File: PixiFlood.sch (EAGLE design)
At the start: 61 parts, among them IC1 L78LXXCU/BU, IC2 74LVC1G125DBV, IC3 LM1117-SOT223, IC4 WS2811SOP8, IC5 TC7W04FP-0.65, U1 PT4115B89E, U2 PT4115B89E, U3 PT4115B89E, X1 22-23-2041

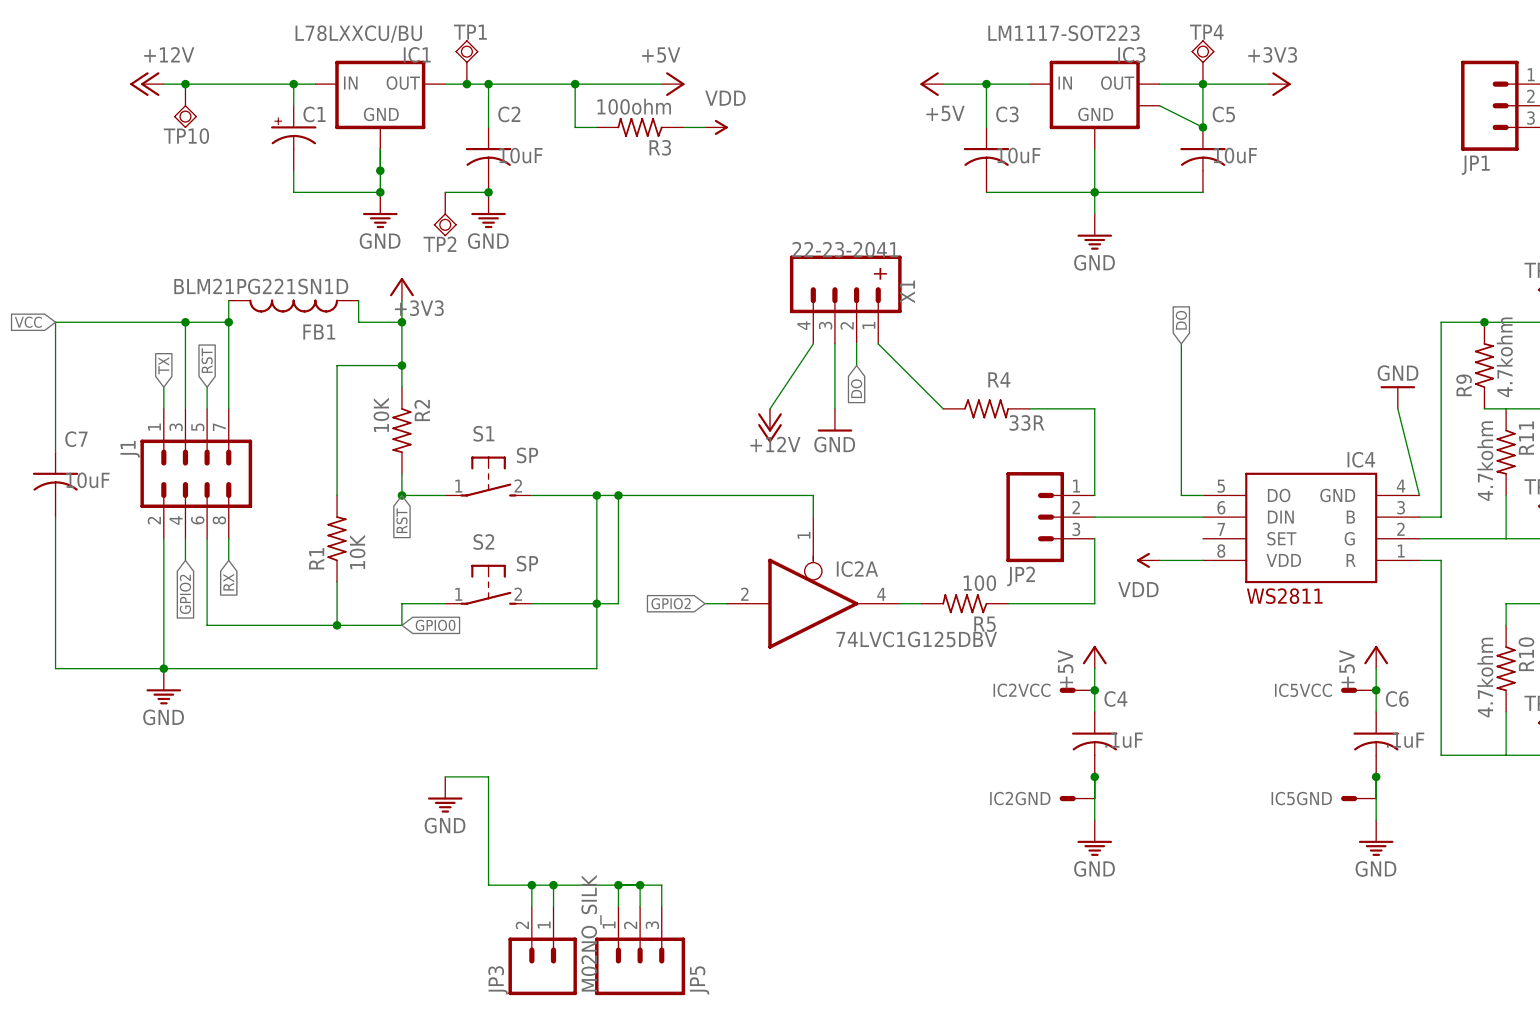
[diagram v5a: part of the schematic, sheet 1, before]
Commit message: Reworked layout
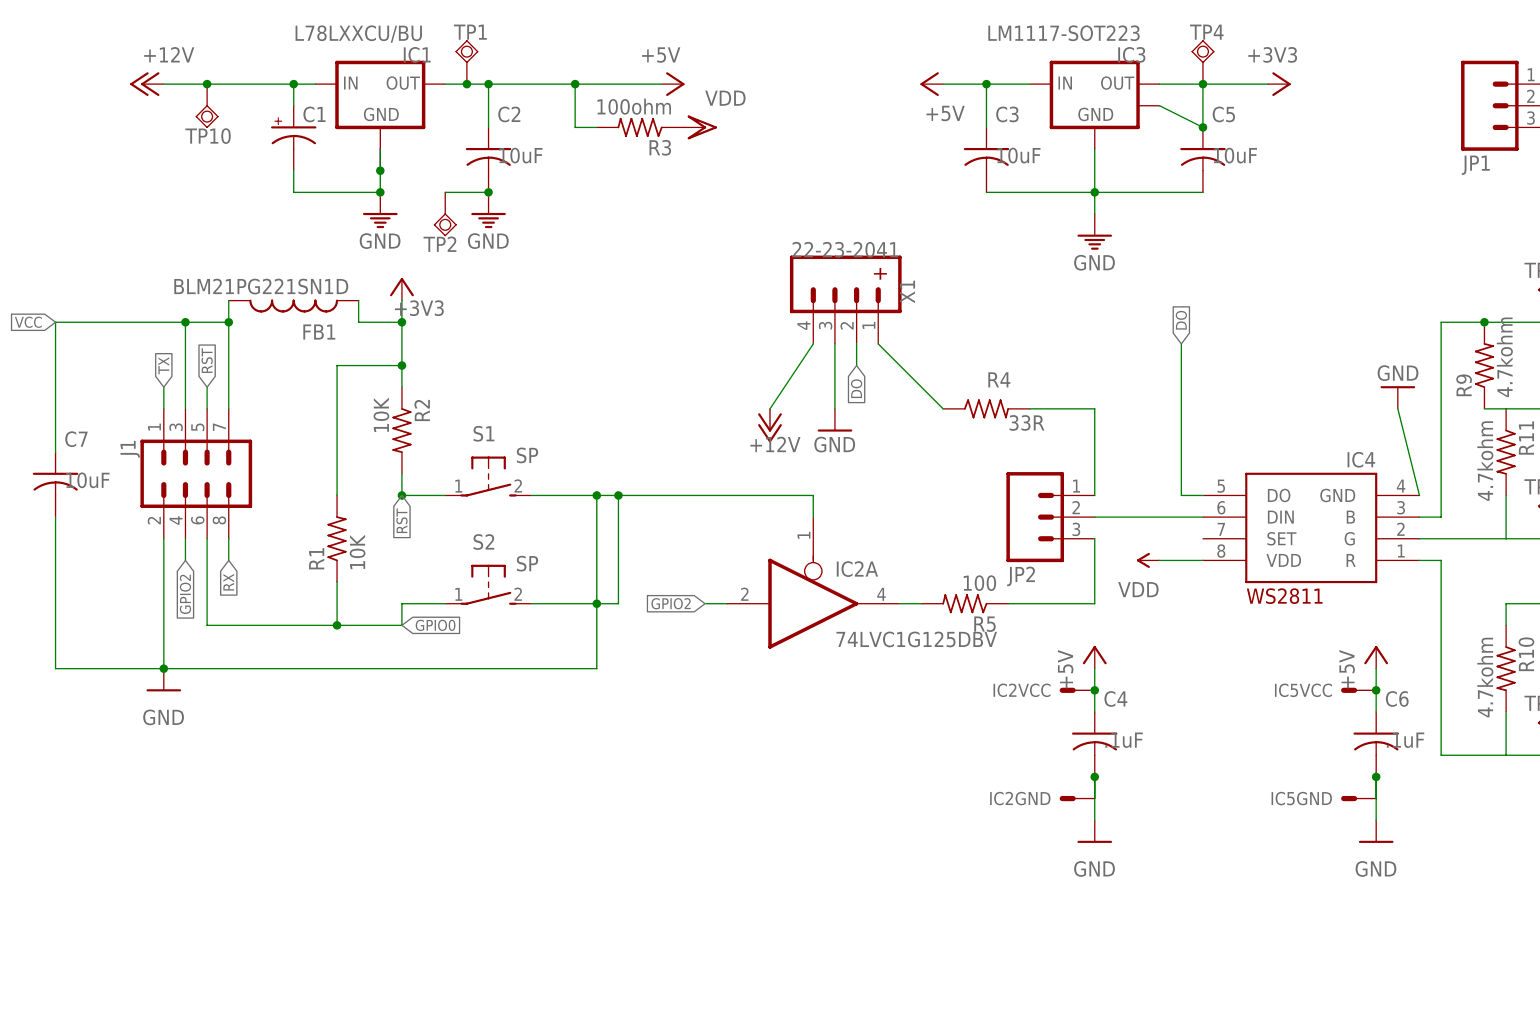
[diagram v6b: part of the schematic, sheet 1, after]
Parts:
- removed JP3: M02NO_SILK, connectors:M02NO_SILK
- removed JP5: (no value), connectors:M03LOCK_NO_SILK
- R3: device rcl:R-US_M0805 -> rcl:R-US_R0805
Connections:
- net GND: no longer JP3.1, JP3.2, JP5.1, JP5.2, JP5.3
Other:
- moved on the sheet: TP10
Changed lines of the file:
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@@
 <part name="P+1" library="supply1" library_urn="urn:adsk.eagle:library:371" deviceset="+12V" device=""/>
 <part name="P+2" library="supply1" library_urn="urn:adsk.eagle:library:371" deviceset="+5V" device=""/>
-<part name="R3" library="rcl" deviceset="R-US_" device="M0805" value="100ohm"/>
+<part name="R3" library="rcl" library_urn="urn:adsk.eagle:library:334" deviceset="R-US_" device="R0805" package3d_urn="urn:adsk.eagle:package:23553/2" value="100ohm"/>
 <part name="IC4" library="drivers" deviceset="WS2811" device="SOP8"/>
 <part name="R4" library="rcl" deviceset="R-US_" device="M1206" value="33R"/>
@@
 <part name="TP9" library="testpad" library_urn="urn:adsk.eagle:library:385" deviceset="TPSQ" device="PAD1-13" package3d_urn="urn:adsk.eagle:package:27946/1" value="TPSQPAD1-13"/>
 <part name="X1" library="connectors" deviceset="22-23-2041" device=""/>
-<part name="SUPPLY1" library="SparkFun-Aesthetics" deviceset="VDD" device=""/>
+<part name="SUPPLY1" library="supply1" library_urn="urn:adsk.eagle:library:371" deviceset="VDD" device=""/>
 <part name="SUPPLY2" library="SparkFun-Aesthetics" deviceset="VDD" device=""/>
 <part name="J1" library="connectors" deviceset="M04X2A" device=""/>
@@
 <part name="R2" library="resistors" deviceset="R-US_" device="R0805" value="10K"/>
 <part name="R5" library="resistors" deviceset="R-US_" device="R0805" value="100"/>
-<part name="GND1" library="supply" deviceset="GND" device=""/>
+<part name="GND1" library="supply1" library_urn="urn:adsk.eagle:library:371" deviceset="GND" device=""/>
 <part name="IC2" library="logic" deviceset="74*1G125" device="DBV" technology="LVC"/>
 <part name="P+5" library="supply1" library_urn="urn:adsk.eagle:library:371" deviceset="+5V" device=""/>
-<part name="GND6" library="supply" deviceset="GND" device=""/>
+<part name="GND6" library="supply1" library_urn="urn:adsk.eagle:library:371" deviceset="GND" device=""/>
 <part name="GND5" library="supply" deviceset="GND" device=""/>
 <part name="GND3" library="supply" deviceset="GND" device=""/>
-<part name="GND10" library="supply" deviceset="GND" device=""/>
-<part name="GND11" library="supply" deviceset="GND" device=""/>
-<part name="GND12" library="supply" deviceset="GND" device=""/>
+<part name="GND10" library="supply1" library_urn="urn:adsk.eagle:library:371" deviceset="GND" device=""/>
+<part name="GND11" library="supply1" library_urn="urn:adsk.eagle:library:371" deviceset="GND" device=""/>
+<part name="GND12" library="supply1" library_urn="urn:adsk.eagle:library:371" deviceset="GND" device=""/>
 <part name="JP2" library="connectors" deviceset="M03" device="LOCK"/>
 <part name="IC1" library="regulators" deviceset="L78LXXCU/BU" device=""/>
@@
 <part name="TP10" library="testpad" library_urn="urn:adsk.eagle:library:385" deviceset="TPSQ" device="PAD1-13" package3d_urn="urn:adsk.eagle:package:27946/1" value="TPSQPAD1-13"/>
 <part name="FB1" library="ELL-i-Passives" deviceset="FB" device="-0805-A" value="BLM21PG221SN1D"/>
-<part name="+3V33" library="supply" deviceset="+3V3" device=""/>
-<part name="+3V32" library="supply" deviceset="+3V3" device=""/>
+<part name="+3V33" library="supply1" library_urn="urn:adsk.eagle:library:371" deviceset="+3V3" device=""/>
+<part name="+3V32" library="supply1" library_urn="urn:adsk.eagle:library:371" deviceset="+3V3" device=""/>
 <part name="GND2" library="supply" deviceset="GND" device=""/>
 <part name="IC3" library="regulators" deviceset="LM1117" device="-SOT223"/>
@@
 <part name="P+6" library="supply1" library_urn="urn:adsk.eagle:library:371" deviceset="+5V" device=""/>
 <part name="C6" library="rcl" library_urn="urn:adsk.eagle:library:334" deviceset="C-US" device="C0805" package3d_urn="urn:adsk.eagle:package:23617/2" value=".1uF"/>
-<part name="GND7" library="supply" deviceset="GND" device=""/>
+<part name="GND7" library="supply1" library_urn="urn:adsk.eagle:library:371" deviceset="GND" device=""/>
 <part name="R9" library="rcl" deviceset="R-US_" device="M0805" value="4.7kohm"/>
 <part name="R10" library="rcl" deviceset="R-US_" device="M0805" value="4.7kohm"/>
@@
 <part name="TP15" library="testpad" library_urn="urn:adsk.eagle:library:385" deviceset="TPSQ" device="PAD1-13" package3d_urn="urn:adsk.eagle:package:27946/1" value="TPSQPAD1-13"/>
 <part name="TP16" library="testpad" library_urn="urn:adsk.eagle:library:385" deviceset="TPSQ" device="PAD1-13" package3d_urn="urn:adsk.eagle:package:27946/1" value="TPSQPAD1-13"/>
-<part name="GND9" library="supply" deviceset="GND" device=""/>
-<part name="JP3" library="connectors" deviceset="M02" device="NO_SILK"/>
-<part name="JP5" library="connectors" deviceset="M03" device="LOCK_NO_SILK"/>
 <part name="C1" library="rcl" library_urn="urn:adsk.eagle:library:334" deviceset="CPOL-US" device="UD-6,3X5,8" package3d_urn="urn:adsk.eagle:package:23471/1"/>
 </parts>
@@
 <attribute name="NAME" x="116.078" y="73.66" size="1.778" layer="95" rot="MR270"/>
 </instance>
-<instance part="SUPPLY1" gate="VDD" x="91.44" y="91.44" smashed="yes" rot="R270">
+<instance part="SUPPLY1" gate="G$1" x="91.44" y="91.44" smashed="yes" rot="R270">
 <attribute name="VALUE" x="91.44" y="93.98" size="1.778" layer="96"/>
 </instance>
@@
 <attribute name="TP_SIGNAL_NAME" x="147.32" y="100.33" size="1.778" layer="97" rot="R180"/>
 </instance>
-<instance part="TP10" gate="G$1" x="30.48" y="93.98" smashed="yes">
-<attribute name="NAME" x="27.94" y="89.535" size="1.778" layer="95"/>
-<attribute name="TP_SIGNAL_NAME" x="33.02" y="92.71" size="1.778" layer="97"/>
+<instance part="TP10" gate="G$1" x="33.02" y="93.98" smashed="yes">
+<attribute name="NAME" x="30.48" y="89.535" size="1.778" layer="95"/>
+<attribute name="TP_SIGNAL_NAME" x="35.56" y="92.71" size="1.778" layer="97"/>
 </instance>
 <instance part="FB1" gate="G$1" x="43.18" y="71.12" smashed="yes" rot="R180">
@@
 <attribute name="NAME" x="193.04" y="24.765" size="1.778" layer="95" rot="R180"/>
 <attribute name="TP_SIGNAL_NAME" x="187.96" y="21.59" size="1.778" layer="97" rot="R180"/>
-</instance>
-<instance part="GND9" gate="1" x="60.96" y="12.7" smashed="yes">
-<attribute name="VALUE" x="58.42" y="8.636" size="1.778" layer="96"/>
-</instance>
-<instance part="JP3" gate="G$1" x="73.66" y="-7.62" smashed="yes" rot="R90">
-<attribute name="VALUE" x="78.74" y="-10.16" size="1.778" layer="96" rot="R90"/>
-<attribute name="NAME" x="67.818" y="-10.16" size="1.778" layer="95" rot="R90"/>
-</instance>
-<instance part="JP5" gate="G$1" x="83.82" y="-7.62" smashed="yes" rot="MR90">
-<attribute name="VALUE" x="76.2" y="-10.16" size="1.778" layer="96" rot="MR90"/>
-<attribute name="NAME" x="89.662" y="-10.16" size="1.778" layer="95" rot="MR90"/>
 </instance>
 <instance part="C1" gate="G$1" x="43.18" y="91.44" smashed="yes">
@@
 <wire x1="170.18" y1="15.24" x2="170.18" y2="12.7" width="0.1524" layer="91"/>
 </segment>
-<segment>
-<pinref part="GND9" gate="1" pin="GND"/>
-<wire x1="60.96" y1="15.24" x2="66.04" y2="15.24" width="0.2032" layer="91"/>
-<wire x1="66.04" y1="15.24" x2="66.04" y2="2.54" width="0.2032" layer="91"/>
-<pinref part="JP3" gate="G$1" pin="2"/>
-<wire x1="66.04" y1="2.54" x2="71.12" y2="2.54" width="0.2032" layer="91"/>
-<wire x1="71.12" y1="0" x2="71.12" y2="2.54" width="0.2032" layer="91"/>
-<pinref part="JP3" gate="G$1" pin="1"/>
-<wire x1="71.12" y1="2.54" x2="73.66" y2="2.54" width="0.2032" layer="91"/>
-<wire x1="73.66" y1="2.54" x2="73.66" y2="0" width="0.2032" layer="91"/>
-<junction x="71.12" y="2.54"/>
-<junction x="73.66" y="2.54"/>
-<pinref part="JP5" gate="G$1" pin="3"/>
-<wire x1="73.66" y1="2.54" x2="83.82" y2="2.54" width="0.2032" layer="91"/>
-<wire x1="81.28" y1="2.54" x2="83.82" y2="2.54" width="0.2032" layer="91"/>
-<wire x1="83.82" y1="2.54" x2="86.36" y2="2.54" width="0.2032" layer="91"/>
-<wire x1="86.36" y1="2.54" x2="86.36" y2="0" width="0.2032" layer="91"/>
-<pinref part="JP5" gate="G$1" pin="2"/>
-<wire x1="83.82" y1="0" x2="83.82" y2="2.54" width="0.2032" layer="91"/>
-<pinref part="JP5" gate="G$1" pin="1"/>
-<wire x1="81.28" y1="0" x2="81.28" y2="2.54" width="0.2032" layer="91"/>
-<junction x="81.28" y="2.54"/>
-<junction x="83.82" y="2.54"/>
-</segment>
 </net>
 <net name="RED" class="0">
@@
 <segment>
 <pinref part="P+1" gate="1" pin="+12V"/>
-<wire x1="27.94" y1="96.52" x2="30.48" y2="96.52" width="0.1524" layer="91"/>
+<wire x1="27.94" y1="96.52" x2="33.02" y2="96.52" width="0.1524" layer="91"/>
 <pinref part="IC1" gate="G$1" pin="IN"/>
 <pinref part="TP10" gate="G$1" pin="TP"/>
-<wire x1="30.48" y1="96.52" x2="43.18" y2="96.52" width="0.1524" layer="91"/>
-<junction x="30.48" y="96.52"/>
+<wire x1="33.02" y1="96.52" x2="43.18" y2="96.52" width="0.1524" layer="91"/>
+<junction x="33.02" y="96.52"/>
 <wire x1="43.18" y1="96.52" x2="45.72" y2="96.52" width="0.1524" layer="91"/>
 <wire x1="43.18" y1="93.98" x2="43.18" y2="96.52" width="0.1524" layer="91"/>
@@
 <segment>
 <pinref part="R3" gate="G$1" pin="1"/>
-<pinref part="SUPPLY1" gate="VDD" pin="VDD"/>
-<wire x1="88.9" y1="91.44" x2="91.44" y2="91.44" width="0.1524" layer="91"/>
+<pinref part="SUPPLY1" gate="G$1" pin="VDD"/>
 </segment>
 <segment>
@@
 <wire x1="149.86" y1="53.34" x2="149.86" y2="60.96" width="0.1524" layer="91"/>
 <pinref part="TP6" gate="G$1" pin="TP"/>
-<wire x1="149.86" y1="68.58" x2="149.86" y2="60.96" width="0.1524" layer="91"/>
 <junction x="149.86" y="60.96"/>
 <pinref part="B1" gate="BLUE" pin="P$1"/>
-</segment>
-</net>
+<wire x1="149.86" y1="68.58" x2="149.86" y2="60.96" width="0.1524" layer="91"/>
+</segment>
+</net>

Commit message: Reworked layout
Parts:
- removed TP11, TP12, TP13, TP14, TP15, TP16, TP4, TP5, TP6, TP7, TP8, TP9: TPSQPAD1-13, testpad:TPSQPAD1-13
- added TP17, TP18, TP19, TP20, TP21, TP22, TP23, TP24, TP25, TP26, TP27, TP28, TP29, TP30, TP31: TEST-POINTTP_15TH_THRU, SparkFun-Connectors:TEST-POINTTP_15TH_THRU
- TP1, TP10, TP2, TP3: value TPSQPAD1-13 -> TEST-POINTTP_15TH_THRU; device testpad:TPSQPAD1-13 -> SparkFun-Connectors:TEST-POINTTP_15TH_THRU
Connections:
- net +12V: now also TP17.1, X1.1; no longer TP10.TP, X1.4
- net +3V3: now also TP19.1; no longer TP4.TP
- net +5V: now also TP10.1; no longer TP1.TP
- net BLUE: now also TP20.1; no longer TP11.TP
- net BOUT: now also TP30.1; no longer TP7.TP
- net DIN-W: now also X1.3; no longer X1.1
- net DO: now also X1.4; no longer X1.2
- net GND: now also TP18.1, X1.2; no longer TP2.TP, X1.3
- net GOUT: now also TP29.1; no longer TP5.TP
- net GREEN: now also TP23.1; no longer TP12.TP
- net LED-B-NEG: now also TP31.1; no longer TP6.TP
- net LED-G-NEG: now also TP28.1; no longer TP8.TP
- net LED-R-NEG: now also TP27.1; no longer TP9.TP
- net N$1: now also TP3.1
- net N$16: now also TP21.1; no longer TP14.TP
- net N$2: now also TP1.1
- net N$3: now also TP24.1; no longer TP16.TP
- net N$4: now also TP22.1; no longer TP15.TP
- net N$5: now also TP2.1
- net RED: now also TP25.1; no longer TP13.TP
- net ROUT: now also TP26.1; no longer TP3.TP
